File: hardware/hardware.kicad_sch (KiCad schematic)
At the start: 8 parts

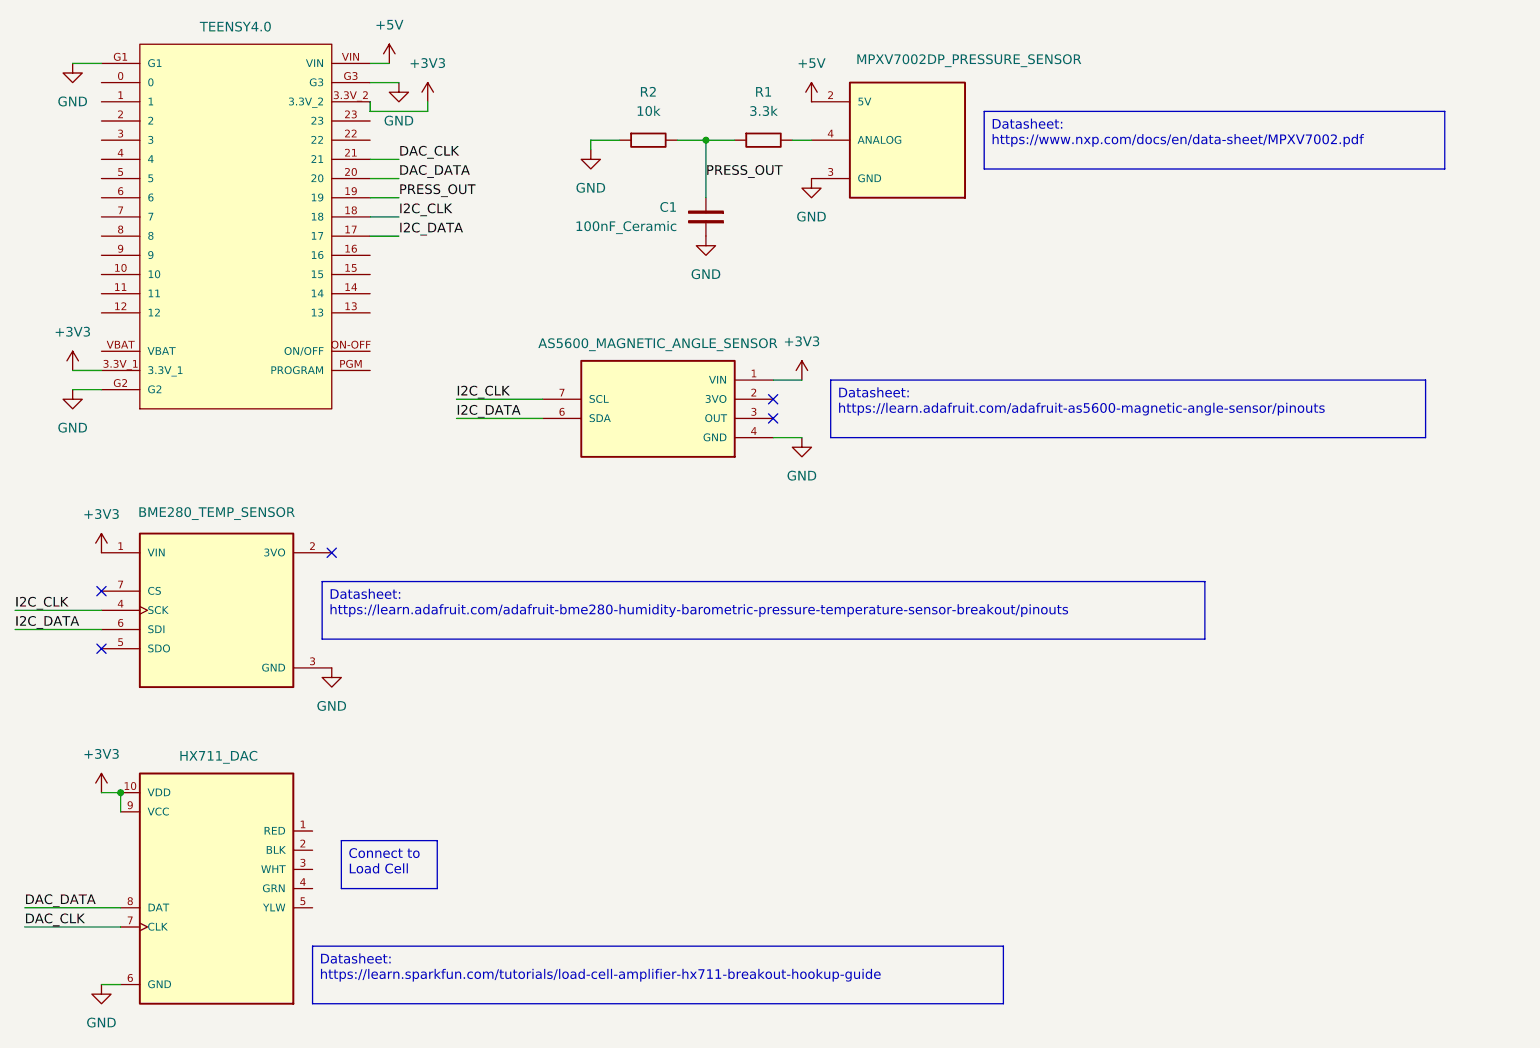
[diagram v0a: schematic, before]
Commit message: changed pin labels
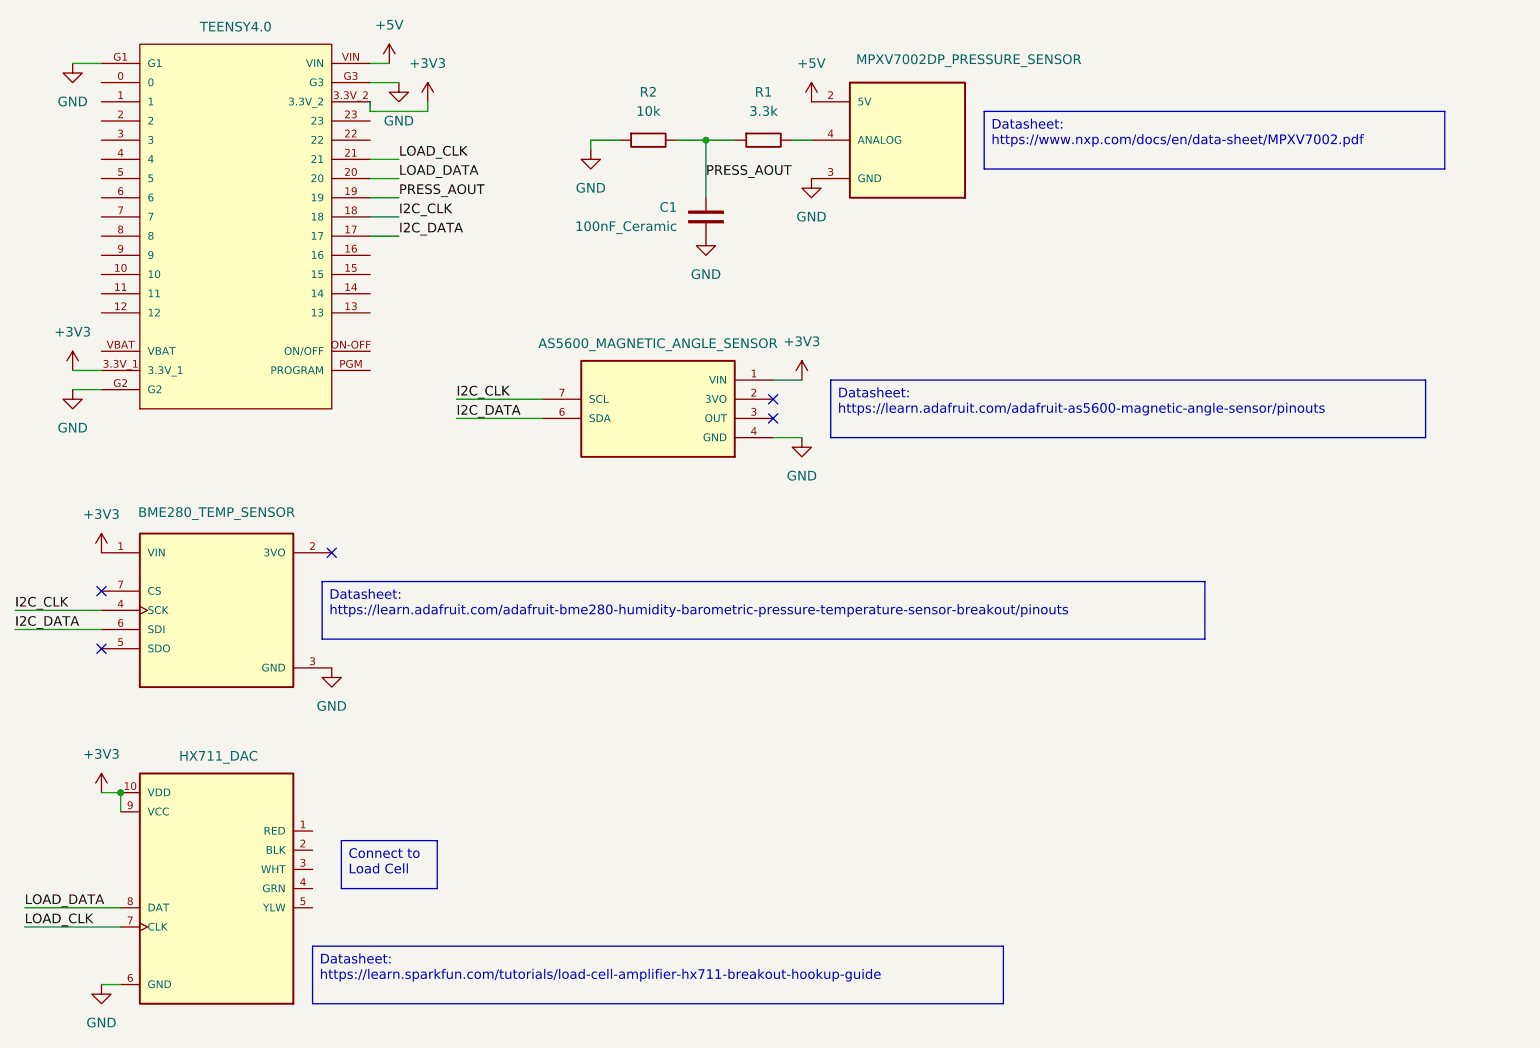
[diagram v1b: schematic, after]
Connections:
- net DAC_CLK renamed LOAD_CLK
- net DAC_DATA renamed LOAD_DATA
- net PRESS_OUT renamed PRESS_AOUT
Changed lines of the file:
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@@
 		)
 	)
-	(label "PRESS_OUT"
+	(label "PRESS_AOUT"
 		(at 140.97 48.26 0)
 		(effects
@@
 		)
 	)
-	(label "DAC_CLK"
+	(label "LOAD_CLK"
 		(at 91.44 144.78 0)
 		(effects
@@
 		)
 	)
-	(label "DAC_DATA"
+	(label "LOAD_DATA"
 		(at 140.97 45.72 0)
 		(effects
@@
 		)
 	)
-	(label "PRESS_OUT"
+	(label "PRESS_AOUT"
 		(at 181.61 45.72 0)
 		(effects
@@
 		)
 	)
-	(label "DAC_CLK"
+	(label "LOAD_CLK"
 		(at 140.97 43.18 0)
 		(effects
@@
 		)
 	)
-	(label "DAC_DATA"
+	(label "LOAD_DATA"
 		(at 91.44 142.24 0)
 		(effects

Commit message: incorporated libraries
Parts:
- renumbered AS5600_MAGNETIC_ANGLE_SENSOR to AS5600_MAGNETIC_ANGLE_SENSOR1, BME280_TEMP_SENSOR to BME280_TEMP_SENSOR1, HX711_DAC to HX711_DAC1, MPXV7002DP_PRESSURE_SENSOR to MPXV7002DP_PRESSURE_SENSOR1
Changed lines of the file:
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@@
 		(on_board yes)
 		(dnp no)
-		(property "Reference" "AS5600_MAGNETIC_ANGLE_SENSOR"
-			(at 175.26 67.564 0)
+		(property "Reference" "AS5600_MAGNETIC_ANGLE_SENSOR1"
+			(at 170.434 67.564 0)
 			(effects
 				(font
@@
 			(project ""
 				(path "/ccca5b34-9e10-49f9-bf4d-4f8efae0db3d"
-					(reference "AS5600_MAGNETIC_ANGLE_SENSOR")
+					(reference "AS5600_MAGNETIC_ANGLE_SENSOR1")
 					(unit 1)
 				)
@@
 		(on_board yes)
 		(dnp no)
-		(property "Reference" "HX711_DAC"
+		(property "Reference" "HX711_DAC1"
 			(at 117.094 122.174 0)
 			(effects
@@
 			(project ""
 				(path "/ccca5b34-9e10-49f9-bf4d-4f8efae0db3d"
-					(reference "HX711_DAC")
+					(reference "HX711_DAC1")
 					(unit 1)
 				)
@@
 		(on_board yes)
 		(dnp no)
-		(property "Reference" "MPXV7002DP_PRESSURE_SENSOR"
+		(property "Reference" "MPXV7002DP_PRESSURE_SENSOR1"
 			(at 216.408 29.972 0)
 			(effects
@@
 			(project ""
 				(path "/ccca5b34-9e10-49f9-bf4d-4f8efae0db3d"
-					(reference "MPXV7002DP_PRESSURE_SENSOR")
+					(reference "MPXV7002DP_PRESSURE_SENSOR1")
 					(unit 1)
 				)
@@
 		(on_board yes)
 		(dnp no)
-		(property "Reference" "BME280_TEMP_SENSOR"
-			(at 116.84 89.916 0)
+		(property "Reference" "BME280_TEMP_SENSOR1"
+			(at 118.872 89.916 0)
 			(effects
 				(font
@@
 			(project ""
 				(path "/ccca5b34-9e10-49f9-bf4d-4f8efae0db3d"
-					(reference "BME280_TEMP_SENSOR")
+					(reference "BME280_TEMP_SENSOR1")
 					(unit 1)
 				)

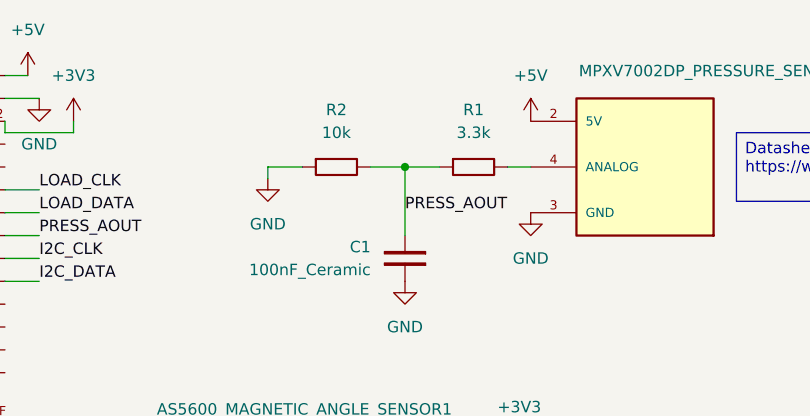
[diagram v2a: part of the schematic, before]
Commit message: Modified embedded to actually work
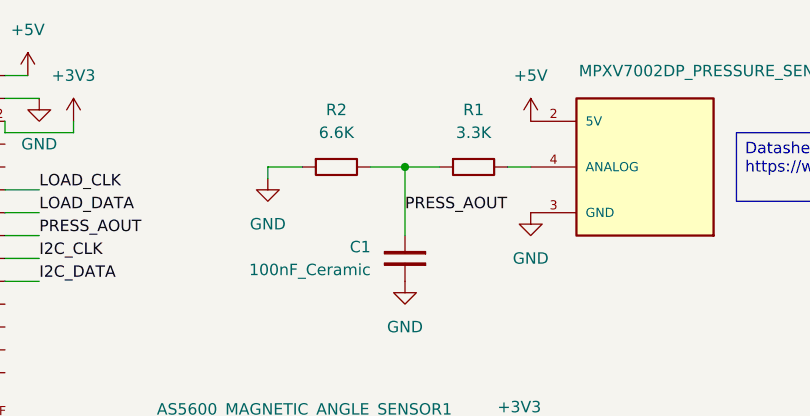
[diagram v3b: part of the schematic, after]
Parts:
- R1: value 3.3k -> 3.3K
- R2: value 10k -> 6.6K
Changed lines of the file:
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@@
 			)
 		)
-		(property "Value" "10k"
+		(property "Value" "6.6K"
 			(at 173.99 36.83 0)
 			(effects
@@
 			)
 		)
-		(property "Value" "3.3k"
+		(property "Value" "3.3K"
 			(at 189.23 36.83 0)
 			(effects

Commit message: won!
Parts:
- added R3: 3.3K, Resistor_THT:R_Axial_DIN0207_L6.3mm_D2.5mm_P10.16mm_Horizontal, symbol SL_Resistors:10k
- C1: value 100nF_Ceramic -> 1uF
- R2: value 6.6K -> 3.3K
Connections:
- net GND: now also R3.1; no longer R2.1
- net I2C_CLK: now also TEENSY4.0.19; no longer TEENSY4.0.18
- net I2C_DATA: now also TEENSY4.0.18; no longer TEENSY4.0.17
- net LOAD_CLK: now also TEENSY4.0.22; no longer TEENSY4.0.21
- net LOAD_DATA: now also TEENSY4.0.21; no longer TEENSY4.0.20
- net PRESS_AOUT: now also TEENSY4.0.20; no longer TEENSY4.0.19
- new net: R2.1, R3.2
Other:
- moved on the sheet: C1, MPXV7002DP_PRESSURE_SENSOR1, R1, R2
